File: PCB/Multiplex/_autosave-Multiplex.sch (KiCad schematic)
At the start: 20 parts, among them J1+1 Power, J1-1 Power, J2+1 I2C, J2-1 I2C, J3 Signal, J4 Track, K1 IM03, Q1 2N7002, U1 PIC16F1503-IP

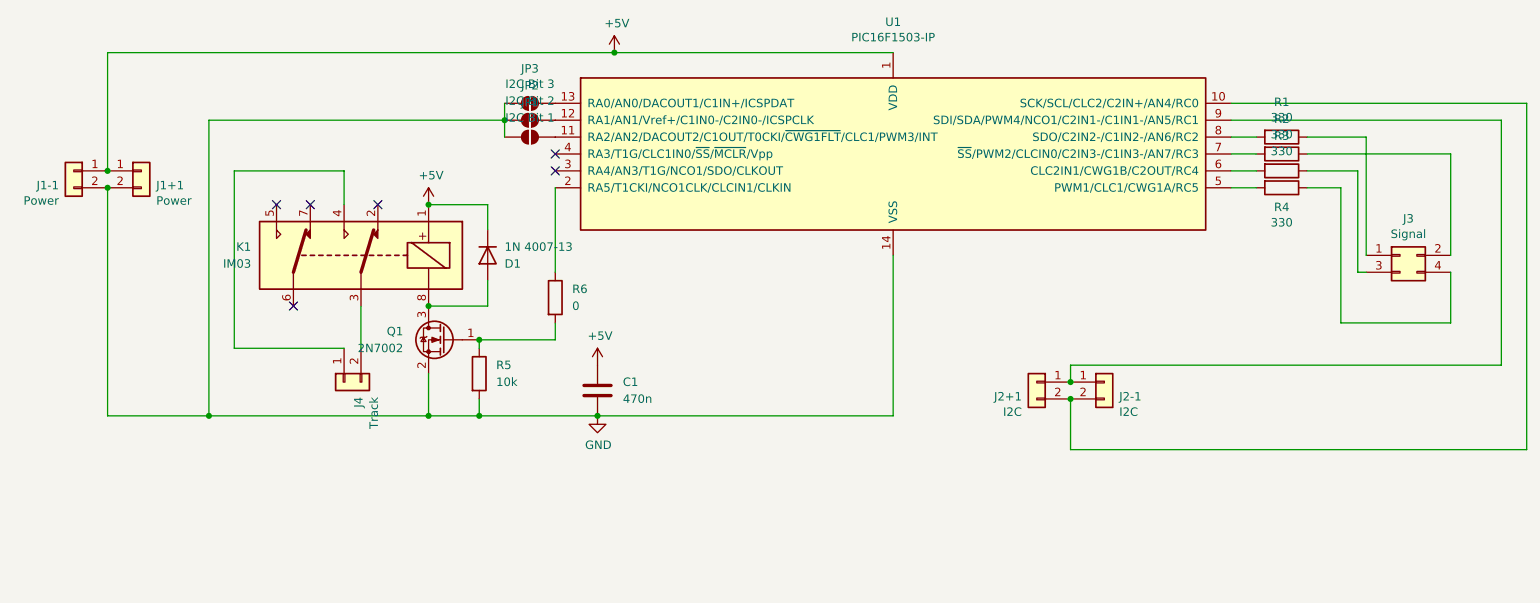
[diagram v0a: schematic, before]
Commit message: Update PCBs and add track occupation PCB.
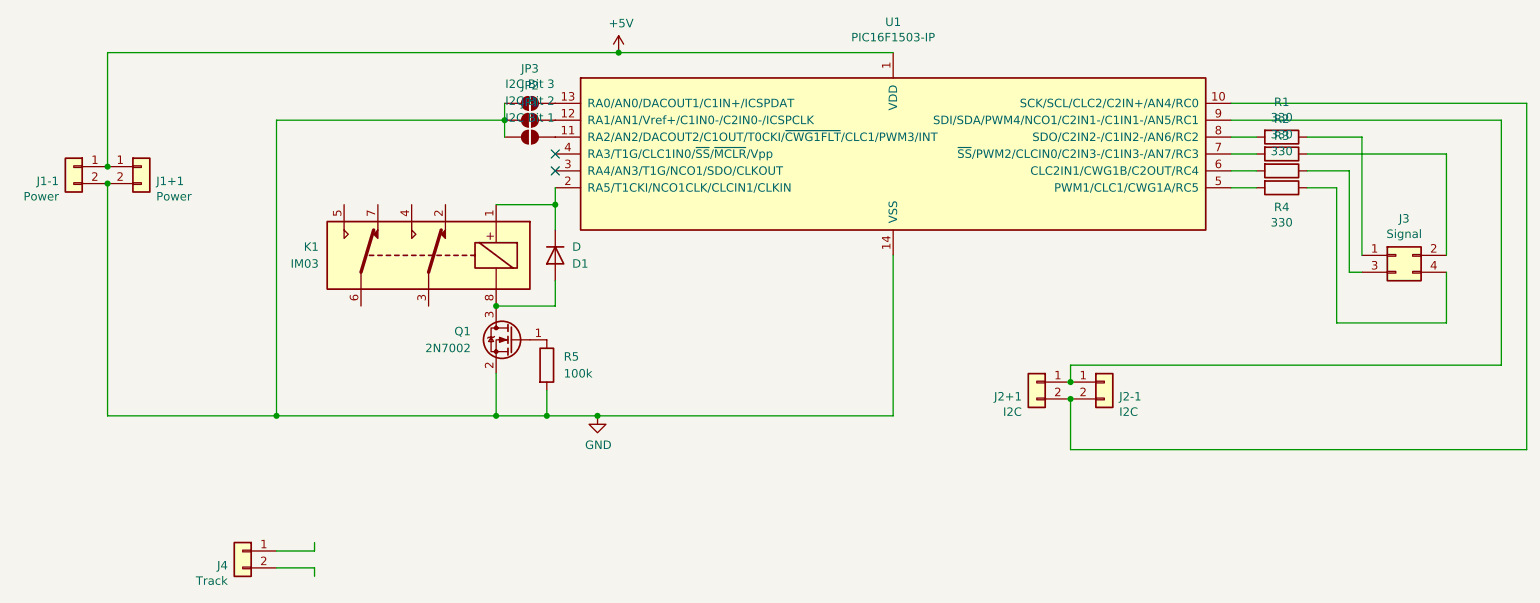
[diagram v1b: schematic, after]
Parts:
- removed C1: 470n, Capacitor_THT:C_Disc_D4.3mm_W1.9mm_P5.00mm, symbol Device:C
- removed R6: 0, Resistor_SMD:R_0603_1608Metric_Pad0.98x0.95mm_HandSolder, symbol Device:R
- D1: value 1N 4007-13 -> D; footprint Diode_THT:D_DO-41_SOD81_P7.62mm_Horizontal -> (none)
- J4: footprint Connector_PinHeader_2.54mm:PinHeader_1x02_P2.54mm_Horizontal -> Connector_PinSocket_2.54mm:PinSocket_1x02_P2.54mm_Horizontal
- K1: footprint Relay_SMD:Relay_2P2T_10x6mm_TE_IMxxG -> (none)
- R1, R2, R3, R4: footprint Resistor_SMD:R_0603_1608Metric_Pad0.98x0.95mm_HandSolder -> Resistor_THT:R_Axial_DIN0207_L6.3mm_D2.5mm_P10.16mm_Horizontal
- R5: value 10k -> 100k; footprint Resistor_SMD:R_0603_1608Metric_Pad0.98x0.95mm_HandSolder -> (none)
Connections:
- net +5V: no longer D1.1 (K), K1.1
- net at U1.2 (RA5/T1CKI/NCO1CLK/CLCIN1/CLKIN): now also D1.1 (K), K1.1
- net at J4.1 (Pin_1): no longer K1.4
- net at J4.2 (Pin_2): no longer K1.3
- no-connect marks 6 -> 2
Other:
- moved on the sheet: D1, J1+1, J1-1, J3, J4, K1, Q1, R5
